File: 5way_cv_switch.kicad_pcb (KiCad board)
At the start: 2 copper layers, 29 x 22 mm, 20 parts, among them J1 I/O connector, J2 5-way Switch Connector, U1 HT7550-1, U2 LMV321IDBVR

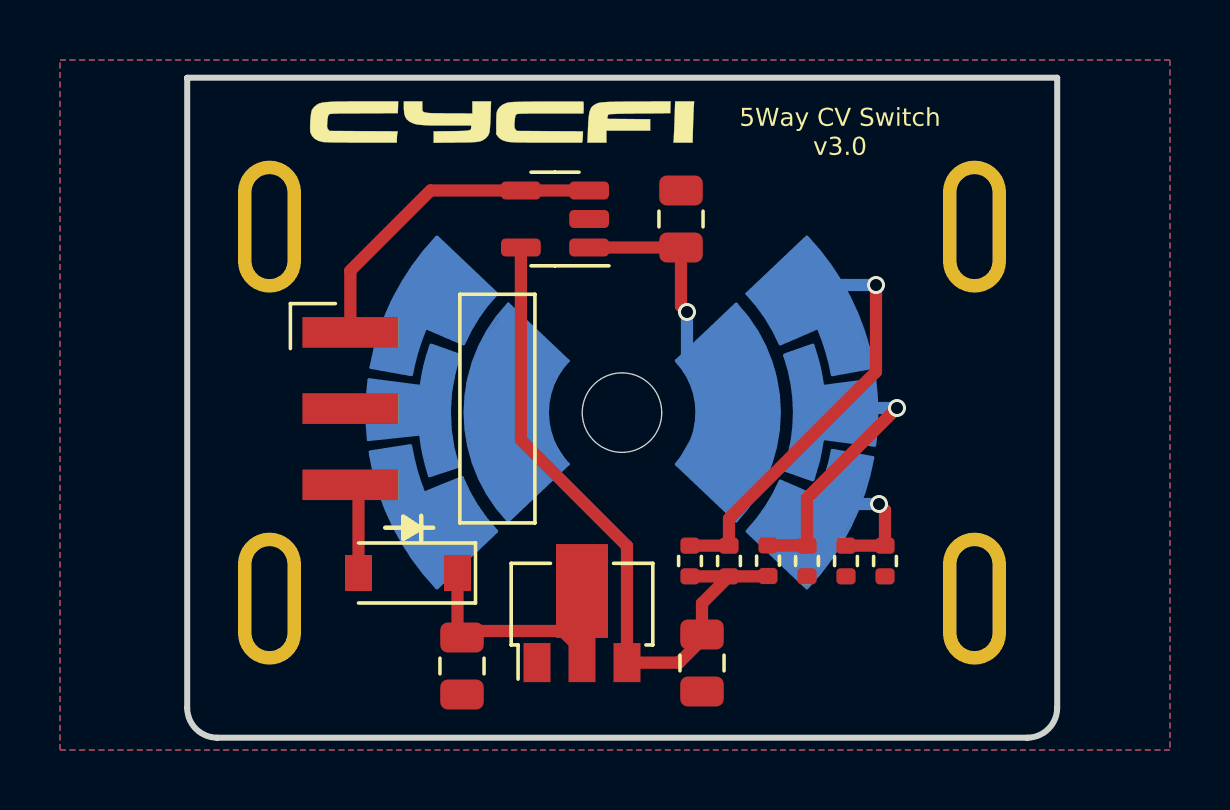
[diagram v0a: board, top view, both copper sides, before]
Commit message: Updates: - Fixed overlapping fill regions when paneling - Added JLCPCB rotation
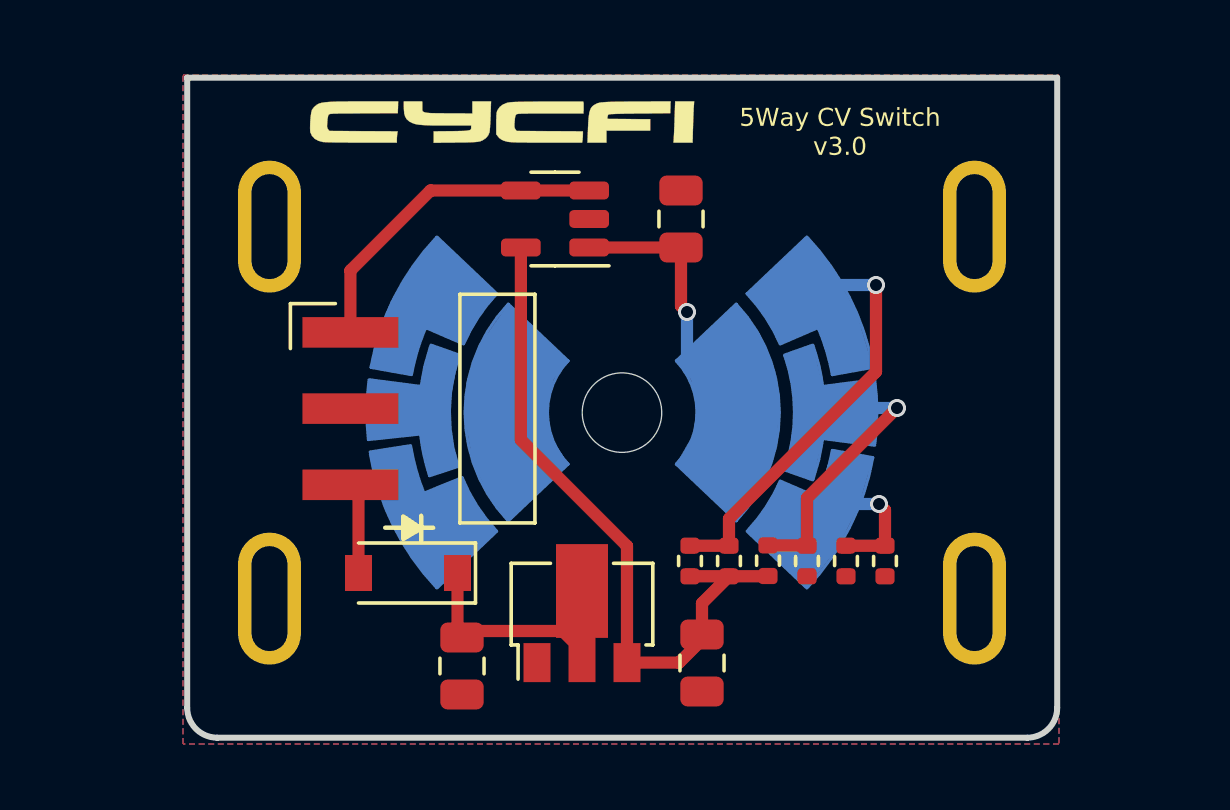
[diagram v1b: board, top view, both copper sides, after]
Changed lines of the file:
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@@
             (gr_line (start -1.012751 -2.540257) (end -2.366089 -2.297148) (width 0.1))
     (gr_arc (start -0.54434 -0.98269) (mid -0.823109 -1.748072) (end -1.012751 -2.540257) (width 0.1))
-    (gr_arc (start -0.18544 2.030115) (mid -1.577032 0.05155) (end -2.355373 -2.238741) (width 0.1))
-    (gr_arc (start 1.829511 0.158474) (mid 1.207925 -0.622296) (end 0.730597 -1.498726) (width 0.1))
+    (gr_arc (start -0.18544 2.030115) (mid -1.577031 0.051552) (end -2.355372 -2.238736) (width 0.1))
+    (gr_arc (start 1.829511 0.158474) (mid 1.207927 -0.622293) (end 0.7306 -1.498719) (width 0.1))
       ))
     (pad "2" smd custom (at -6.9 0 180) (size 1.524 1.524) (layers "B.Cu")
@@
             (xy -1.143 -0.381)
           ) (width 0) (fill yes))
-    (gr_arc (start 1.468521 1.887188) (mid 1.150176 0.005015) (end 1.465238 -1.87771) (width 0.1))
+    (gr_arc (start 1.468521 1.887188) (mid 1.150176 0.005019) (end 1.465236 -1.877703) (width 0.1))
             (gr_line (start 1.478475 -1.915614) (end 0.535602 -2.248764) (width 0.1))
             (gr_line (start 0.535602 2.248763) (end 1.478475 1.915613) (width 0.1))
-    (gr_arc (start 0.210716 -0.903391) (mid 0.334378 -1.567309) (end 0.523935 -2.215498) (width 0.1))
+    (gr_arc (start 0.210716 -0.903391) (mid 0.334378 -1.567307) (end 0.523933 -2.215493) (width 0.1))
             (gr_line (start 0.206103 -0.868475) (end -1.529351 -1.093636) (width 0.1))
-    (gr_arc (start -1.533117 1.064237) (mid -1.60007 0.007419) (end -1.534963 -1.049514) (width 0.1))
+    (gr_arc (start -1.533117 1.064237) (mid -1.60006 0.014829) (end -1.536782 -1.034806) (width 0.1))
             (gr_line (start -1.529351 1.093635) (end 0.206103 0.868475) (width 0.1))
-    (gr_arc (start 0.527809 2.226602) (mid 0.334386 1.567344) (end 0.209164 0.891804) (width 0.1))
+    (gr_arc (start 0.527809 2.226602) (mid 0.335751 1.573051) (end 0.210722 0.903437) (width 0.1))
             (gr_poly (pts
             (xy 1.478475 1.915613)
@@
             (gr_line (start 1.929527 -0.158491) (end -0.065048 -2.051683) (width 0.1))
             (gr_line (start -2.266089 2.297148) (end -0.912751 2.540256) (width 0.1))
-    (gr_arc (start -0.90831 2.515788) (mid -0.724899 1.754037) (end -0.459005 1.017013) (width 0.1))
+    (gr_arc (start -0.90831 2.515788) (mid -0.7249 1.754041) (end -0.459008 1.017021) (width 0.1))
     (gr_arc (start -2.263448 2.282536) (mid -1.487096 -0.031688) (end -0.085439 -2.030116) (width 0.1))
-    (gr_arc (start 0.830582 1.498761) (mid 1.294101 0.643249) (end 1.895138 -0.121934) (width 0.1))
+    (gr_arc (start 0.830582 1.498761) (mid 1.294101 0.64325) (end 1.895137 -0.121933) (width 0.1))
       ))
     (pad "4" smd custom (at -3.8 0 180) (size 1.524 1.524) (layers "B.Cu")
@@
             (gr_line (start 1.139203 2.797621) (end 2.497646 2.584881) (width 0.1))
             (gr_line (start 0.265047 -1.951683) (end -1.729527 -0.058491) (width 0.1))
-    (gr_arc (start 0.285433 -1.930128) (mid 1.716564 0.126825) (end 2.485847 2.511651) (width 0.1))
-    (gr_arc (start 0.712637 1.246919) (mid 0.964993 1.99224) (end 1.133367 2.760899) (width 0.1))
+    (gr_arc (start 0.285433 -1.930128) (mid 1.716562 0.126822) (end 2.485846 2.511644) (width 0.1))
+    (gr_arc (start 0.712637 1.246919) (mid 0.963331 1.986268) (end 1.131378 2.748662) (width 0.1))
     (gr_arc (start -1.715715 -0.043877) (mid -1.063286 0.790947) (end -0.574737 1.731114) (width 0.1))
       ))
@@
           ) (width 0) (fill yes))
             (gr_line (start -0.606104 0.768475) (end 1.129351 0.993635) (width 0.1))
-    (gr_arc (start -0.607622 0.780122) (mid -0.730321 1.450207) (end -0.920107 2.104462) (width 0.1))
+    (gr_arc (start -0.607622 0.780122) (mid -0.728977 1.444498) (end -0.916283 2.093374) (width 0.1))
             (gr_line (start -1.878476 1.815613) (end -0.935602 2.148763) (width 0.1))
-    (gr_arc (start -1.82922 -1.870054) (mid -1.550187 -0.043229) (end -1.865234 1.777731) (width 0.1))
+    (gr_arc (start -1.82922 -1.870054) (mid -1.550187 -0.04323) (end -1.865233 1.777728) (width 0.1))
             (gr_line (start -0.888744 -2.211467) (end -1.83856 -1.898657) (width 0.1))
-    (gr_arc (start 1.151731 -1.004571) (mid 1.199614 -0.019644) (end 1.133117 0.964201) (width 0.1))
+    (gr_arc (start 1.151731 -1.004571) (mid 1.199681 -0.027057) (end 1.13496 0.949489) (width 0.1))
             (gr_line (start 1.151729 -1.004589) (end -0.588333 -0.81835) (width 0.1))
     (gr_arc (start -0.881411 -2.189057) (mid -0.70049 -1.517087) (end -0.589601 -0.83008) (width 0.1))
@@
             (gr_line (start 0.539414 -1.071276) (end -0.722578 -1.61717) (width 0.1))
             (gr_line (start 2.366088 -2.397148) (end 1.01275 -2.640257) (width 0.1))
-    (gr_arc (start -0.734602 -1.589582) (mid -1.199616 -0.734871) (end -1.801991 0.02927) (width 0.1))
+    (gr_arc (start -0.734602 -1.589582) (mid -1.196854 -0.739065) (end -1.795136 0.021931) (width 0.1))
     (gr_arc (start 2.363447 -2.382536) (mid 1.587095 -0.068312) (end 0.185438 1.930116) (width 0.1))
-    (gr_arc (start 1.008309 -2.615789) (mid 0.824898 -1.854038) (end 0.559004 -1.117014) (width 0.1))
+    (gr_arc (start 1.008309 -2.615789) (mid 0.824899 -1.854042) (end 0.559007 -1.117022) (width 0.1))
       ))
     (pad "8" smd custom (at 3.68 -0.1 180) (size 1.524 1.524) (layers "B.Cu")
@@
     (polygon
       (pts
-        (xy 167.76 60.41)
-        (xy 130.76 60.41)
-        (xy 130.76 37.41)
-        (xy 167.76 37.41)
+        (xy 164.06 60.21)
+        (xy 134.86 60.21)
+        (xy 134.86 37.91)
+        (xy 164.06 37.91)
       )
     )
@@
     (polygon
       (pts
-        (xy 167.76 60.41)
-        (xy 130.76 60.41)
-        (xy 130.76 37.41)
-        (xy 167.76 37.41)
+        (xy 164.06 60.21)
+        (xy 134.86 60.21)
+        (xy 134.86 37.91)
+        (xy 164.06 37.91)
       )
     )
